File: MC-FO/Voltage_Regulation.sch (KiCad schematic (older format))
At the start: 2 parts

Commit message: Add files via upload
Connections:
- net GND renamed GND1
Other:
- note added: "add comparatorson both and logically AND together for LED on power status\n\n\n (windowed comparators or voltage supervisors)"
- note added: "zach planning on adding caps. Pi Filter"
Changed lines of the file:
@@
 $Descr A4 11693 8268
 encoding utf-8
-Sheet 2 12
+Sheet 11 11
 Title ""
 Date ""
@@
 Wire Wire Line
 	3600 5150 4150 5150
-Text GLabel 4150 5150 2    50   Input ~ 0
-5V
-$Comp
-L power:GND #PWR?
-U 1 1 61717715
-P 3300 4900
-F 0 "#PWR?" H 3300 4650 50  0001 C CNN
-F 1 "GND" H 3305 4727 50  0000 C CNN
-F 2 "" H 3300 4900 50  0001 C CNN
-F 3 "" H 3300 4900 50  0001 C CNN
-	1    3300 4900
-	1    0    0    -1
-$EndComp
 Wire Wire Line
 	5950 4700 5650 4700
@@
 Wire Wire Line
 	5950 5150 6500 5150
-Text GLabel 6500 5150 2    50   Input ~ 0
-3V3
-$Comp
-L power:GND #PWR?
-U 1 1 6171CE7D
-P 5650 4900
-F 0 "#PWR?" H 5650 4650 50  0001 C CNN
-F 1 "GND" H 5655 4727 50  0000 C CNN
-F 2 "" H 5650 4900 50  0001 C CNN
-F 3 "" H 5650 4900 50  0001 C CNN
-	1    5650 4900
-	1    0    0    -1
-$EndComp
 $Comp
 L R-78E3.3-0.5:R-78E3.3-0.5 T?
@@
 Text HLabel 4750 3900 0    50   Input ~ 0
 Vdd
+Text Notes 3700 2550 2    50   ~ 0
+add comparatorson both and logically AND together for LED on power status\n\n\n (windowed comparators or voltage supervisors)
+Text Notes 2550 3650 2    50   ~ 0
+zach planning on adding caps. Pi Filter
+Text HLabel 6500 5150 2    50   Input ~ 0
+3V3
+Text HLabel 4150 5150 2    50   Input ~ 0
+5V
+Text HLabel 3300 4900 0    50   Input ~ 0
+GND1
+Text HLabel 5650 4900 0    50   Input ~ 0
+GND1
 $EndSCHEMATC

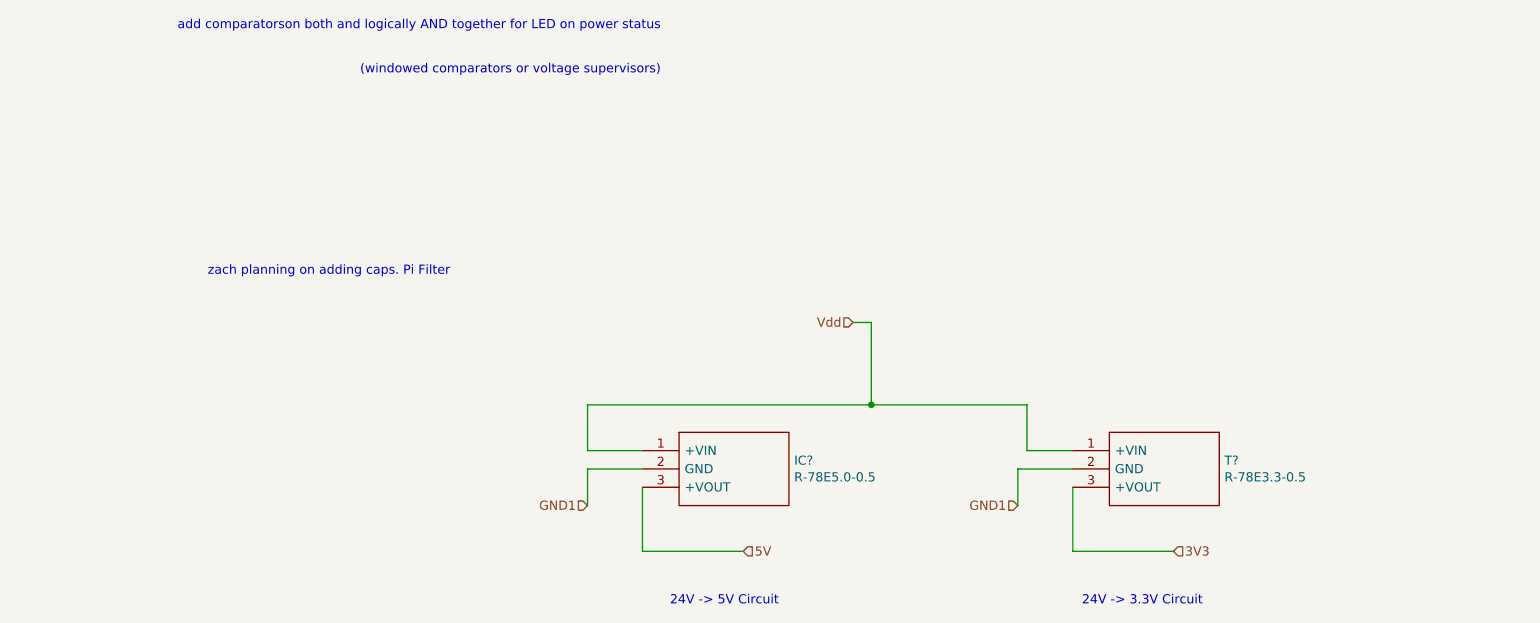
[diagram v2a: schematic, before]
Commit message: Updated naming, Pi filters
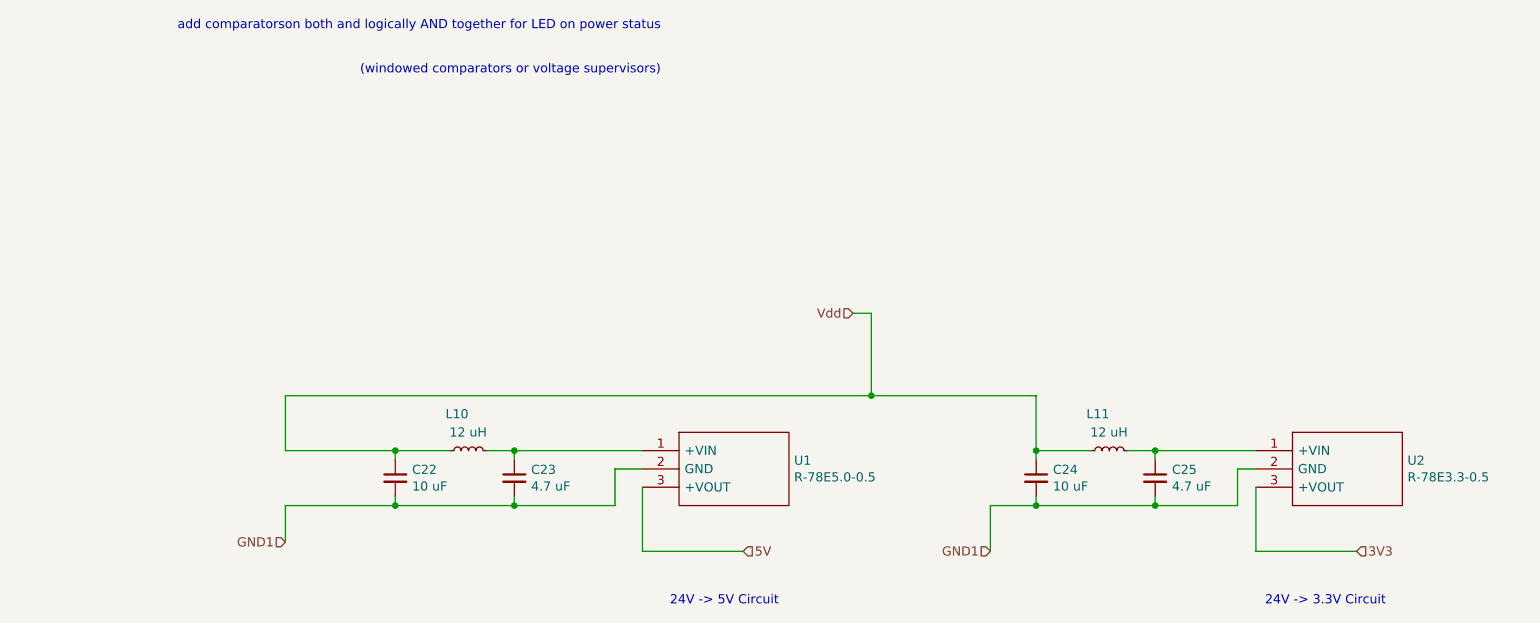
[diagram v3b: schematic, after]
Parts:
- added C22, C24: 10 uF, symbol Device:C_Small
- added C23, C25: 4.7 uF, symbol Device:C_Small
- added L10, L11: 12 uH, symbol Device:L_Small
- gave numbers to parts that had none: 2
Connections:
- net GND1: now also C22.2, C23.2, C24.2, C25.2
- net Vdd: now also C22.1, C24.1, L10.1, L11.1; no longer U1.1 (+VIN), U2.1 (+VIN)
- new net: C23.1, L10.2, U1.1 (+VIN)
- new net: C25.1, L11.2, U2.1 (+VIN)
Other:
- note removed: "zach planning on adding caps. Pi Filter"
- moved on the sheet: U2
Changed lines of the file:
@@
 $Descr A4 11693 8268
 encoding utf-8
-Sheet 11 11
+Sheet 10 11
 Title ""
 Date ""
@@
 Text Notes 3750 5450 0    50   ~ 0
 24V -> 5V Circuit
-Text Notes 6000 5450 0    50   ~ 0
+Text Notes 7000 5450 0    50   ~ 0
 24V -> 3.3V Circuit
 $Comp
@@
 U 1 1 61715B51
 P 3600 4600
-F 0 "IC?" H 4428 4546 50  0000 L CNN
+AR Path="/61715B51" Ref="IC?"  Part="1"
+AR Path="/6175C442/61715B51" Ref="U1"  Part="1"
+F 0 "U1" H 4428 4546 50  0000 L CNN
 F 1 "R-78E5.0-0.5" H 4428 4455 50  0000 L CNN
 F 2 "R78E5005" H 4450 4700 50  0001 L CNN
@@
 $EndComp
 Wire Wire Line
-	3600 4700 3300 4700
-Wire Wire Line
-	3300 4700 3300 4900
+	1650 4900 1650 5100
 Wire Wire Line
 	3600 4800 3600 5150
@@
 	3600 5150 4150 5150
 Wire Wire Line
-	5950 4700 5650 4700
-Wire Wire Line
-	5650 4700 5650 4900
-Wire Wire Line
-	5950 4800 5950 5150
-Wire Wire Line
-	5950 5150 6500 5150
+	6950 4800 6950 5150
+Wire Wire Line
+	6950 5150 7500 5150
 $Comp
 L R-78E3.3-0.5:R-78E3.3-0.5 T?
 U 1 1 6171D286
-P 5950 4600
-F 0 "T?" H 6778 4546 50  0000 L CNN
-F 1 "R-78E3.3-0.5" H 6778 4455 50  0000 L CNN
-F 2 "R78E1205" H 6800 4700 50  0001 L CNN
-F 3 "http://www.recom-power.com/pdf/Innoline/R-78Exx-0.5.pdf" H 6800 4600 50  0001 L CNN
-	1    5950 4600
-	1    0    0    -1
-$EndComp
-Wire Wire Line
-	4750 3900 4850 3900
-Wire Wire Line
-	4850 3900 4850 4350
-Wire Wire Line
-	4850 4350 3300 4350
-Wire Wire Line
-	3300 4350 3300 4600
-Wire Wire Line
-	3300 4600 3600 4600
-Wire Wire Line
-	4850 4350 5700 4350
-Wire Wire Line
-	5700 4350 5700 4600
-Connection ~ 4850 4350
-Wire Wire Line
-	5700 4600 5950 4600
-Text HLabel 4750 3900 0    50   Input ~ 0
+P 6950 4600
+AR Path="/6171D286" Ref="T?"  Part="1"
+AR Path="/6175C442/6171D286" Ref="U2"  Part="1"
+F 0 "U2" H 7778 4546 50  0000 L CNN
+F 1 "R-78E3.3-0.5" H 7778 4455 50  0000 L CNN
+F 2 "R78E1205" H 7800 4700 50  0001 L CNN
+F 3 "http://www.recom-power.com/pdf/Innoline/R-78Exx-0.5.pdf" H 7800 4600 50  0001 L CNN
+	1    6950 4600
+	1    0    0    -1
+$EndComp
+Wire Wire Line
+	4750 3850 4850 3850
+Wire Wire Line
+	4850 3850 4850 4300
+Connection ~ 4850 4300
+Text HLabel 4750 3850 0    50   Input ~ 0
 Vdd
 Text Notes 3700 2550 2    50   ~ 0
 add comparatorson both and logically AND together for LED on power status\n\n\n (windowed comparators or voltage supervisors)
-Text Notes 2550 3650 2    50   ~ 0
-zach planning on adding caps. Pi Filter
-Text HLabel 6500 5150 2    50   Input ~ 0
+Text HLabel 7500 5150 2    50   Input ~ 0
 3V3
 Text HLabel 4150 5150 2    50   Input ~ 0
 5V
-Text HLabel 3300 4900 0    50   Input ~ 0
+Text HLabel 1650 5100 0    50   Input ~ 0
 GND1
-Text HLabel 5650 4900 0    50   Input ~ 0
+Text HLabel 5500 5150 0    50   Input ~ 0
 GND1
+$Comp
+L Device:C_Small C22
+U 1 1 61765AF4
+P 2250 4750
+F 0 "C22" H 2342 4796 50  0000 L CNN
+F 1 "10 uF" H 2342 4705 50  0000 L CNN
+F 2 "" H 2250 4750 50  0001 C CNN
+F 3 "~" H 2250 4750 50  0001 C CNN
+	1    2250 4750
+	1    0    0    -1
+$EndComp
+$Comp
+L Device:C_Small C23
+U 1 1 61766D82
+P 2900 4750
+F 0 "C23" H 2992 4796 50  0000 L CNN
+F 1 "4.7 uF" H 2992 4705 50  0000 L CNN
+F 2 "" H 2900 4750 50  0001 C CNN
+F 3 "~" H 2900 4750 50  0001 C CNN
+	1    2900 4750
+	1    0    0    -1
+$EndComp
+$Comp
+L Device:L_Small L10
+U 1 1 61767909
+P 2650 4600
+F 0 "L10" V 2850 4600 50  0000 L CNN
+F 1 "12 uH" V 2750 4500 50  0000 L CNN
+F 2 "" H 2650 4600 50  0001 C CNN
+F 3 "~" H 2650 4600 50  0001 C CNN
+	1    2650 4600
+	0    -1   -1   0
+$EndComp
+Wire Wire Line
+	1650 4300 4850 4300
+Wire Wire Line
+	2550 4600 2250 4600
+Wire Wire Line
+	2250 4600 2250 4650
+Wire Wire Line
+	2250 4600 1650 4600
+Connection ~ 2250 4600
+Wire Wire Line
+	2750 4600 2900 4600
+Wire Wire Line
+	2900 4600 2900 4650
+Wire Wire Line
+	2900 4600 3600 4600
+Connection ~ 2900 4600
+Wire Wire Line
+	2250 4900 2250 4850
+Wire Wire Line
+	1650 4900 2250 4900
+Wire Wire Line
+	2250 4900 2900 4900
+Wire Wire Line
+	2900 4900 2900 4850
+Connection ~ 2250 4900
+Wire Wire Line
+	2900 4900 3450 4900
+Wire Wire Line
+	3450 4900 3450 4700
+Wire Wire Line
+	3450 4700 3600 4700
+Connection ~ 2900 4900
+Wire Wire Line
+	1650 4300 1650 4600
+$Comp
+L Device:C_Small C24
+U 1 1 61773A69
+P 5750 4750
+F 0 "C24" H 5842 4796 50  0000 L CNN
+F 1 "10 uF" H 5842 4705 50  0000 L CNN
+F 2 "" H 5750 4750 50  0001 C CNN
+F 3 "~" H 5750 4750 50  0001 C CNN
+	1    5750 4750
+	1    0    0    -1
+$EndComp
+$Comp
+L Device:C_Small C25
+U 1 1 61773ADF
+P 6400 4750
+F 0 "C25" H 6492 4796 50  0000 L CNN
+F 1 "4.7 uF" H 6492 4705 50  0000 L CNN
+F 2 "" H 6400 4750 50  0001 C CNN
+F 3 "~" H 6400 4750 50  0001 C CNN
+	1    6400 4750
+	1    0    0    -1
+$EndComp
+$Comp
+L Device:L_Small L11
+U 1 1 61773AE9
+P 6150 4600
+F 0 "L11" V 6350 4600 50  0000 L CNN
+F 1 "12 uH" V 6250 4500 50  0000 L CNN
+F 2 "" H 6150 4600 50  0001 C CNN
+F 3 "~" H 6150 4600 50  0001 C CNN
+	1    6150 4600
+	0    -1   -1   0
+$EndComp
+Wire Wire Line
+	6050 4600 5750 4600
+Wire Wire Line
+	5750 4600 5750 4650
+Wire Wire Line
+	6250 4600 6400 4600
+Wire Wire Line
+	6400 4600 6400 4650
+Wire Wire Line
+	5750 4900 5750 4850
+Wire Wire Line
+	5750 4900 6400 4900
+Wire Wire Line
+	6400 4900 6400 4850
+Wire Wire Line
+	5500 4900 5750 4900
+Wire Wire Line
+	5500 4900 5500 5150
+Connection ~ 5750 4900
+Wire Wire Line
+	5750 4300 5750 4600
+Wire Wire Line
+	4850 4300 5750 4300
+Connection ~ 5750 4600
+Wire Wire Line
+	6400 4600 6950 4600
+Connection ~ 6400 4600
+Wire Wire Line
+	6400 4900 6850 4900
+Wire Wire Line
+	6850 4900 6850 4700
+Wire Wire Line
+	6850 4700 6950 4700
+Connection ~ 6400 4900
 $EndSCHEMATC

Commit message: Add files via upload
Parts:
- renumbered C22 to C31, C23 to C32, C24 to C33, C25 to C34, U1 to IC1, L10 to L1, L11 to L2, U2 to T1
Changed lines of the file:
@@
 P 3600 4600
 AR Path="/61715B51" Ref="IC?"  Part="1"
-AR Path="/6175C442/61715B51" Ref="U1"  Part="1"
-F 0 "U1" H 4428 4546 50  0000 L CNN
+AR Path="/6175C442/61715B51" Ref="IC1"  Part="1"
+F 0 "IC1" H 4428 4546 50  0000 L CNN
 F 1 "R-78E5.0-0.5" H 4428 4455 50  0000 L CNN
 F 2 "R78E5005" H 4450 4700 50  0001 L CNN
@@
 P 6950 4600
 AR Path="/6171D286" Ref="T?"  Part="1"
-AR Path="/6175C442/6171D286" Ref="U2"  Part="1"
-F 0 "U2" H 7778 4546 50  0000 L CNN
+AR Path="/6175C442/6171D286" Ref="T1"  Part="1"
+F 0 "T1" H 7778 4546 50  0000 L CNN
 F 1 "R-78E3.3-0.5" H 7778 4455 50  0000 L CNN
 F 2 "R78E1205" H 7800 4700 50  0001 L CNN
@@
 GND1
 $Comp
-L Device:C_Small C22
+L Device:C_Small C31
 U 1 1 61765AF4
 P 2250 4750
-F 0 "C22" H 2342 4796 50  0000 L CNN
+F 0 "C31" H 2342 4796 50  0000 L CNN
 F 1 "10 uF" H 2342 4705 50  0000 L CNN
 F 2 "" H 2250 4750 50  0001 C CNN
@@
 $EndComp
 $Comp
-L Device:C_Small C23
+L Device:C_Small C32
 U 1 1 61766D82
 P 2900 4750
-F 0 "C23" H 2992 4796 50  0000 L CNN
+F 0 "C32" H 2992 4796 50  0000 L CNN
 F 1 "4.7 uF" H 2992 4705 50  0000 L CNN
 F 2 "" H 2900 4750 50  0001 C CNN
@@
 $EndComp
 $Comp
-L Device:L_Small L10
+L Device:L_Small L1
 U 1 1 61767909
 P 2650 4600
-F 0 "L10" V 2850 4600 50  0000 L CNN
+F 0 "L1" V 2850 4600 50  0000 L CNN
 F 1 "12 uH" V 2750 4500 50  0000 L CNN
 F 2 "" H 2650 4600 50  0001 C CNN
@@
 	1650 4300 1650 4600
 $Comp
-L Device:C_Small C24
+L Device:C_Small C33
 U 1 1 61773A69
 P 5750 4750
-F 0 "C24" H 5842 4796 50  0000 L CNN
+F 0 "C33" H 5842 4796 50  0000 L CNN
 F 1 "10 uF" H 5842 4705 50  0000 L CNN
 F 2 "" H 5750 4750 50  0001 C CNN
@@
 $EndComp
 $Comp
-L Device:C_Small C25
+L Device:C_Small C34
 U 1 1 61773ADF
 P 6400 4750
-F 0 "C25" H 6492 4796 50  0000 L CNN
+F 0 "C34" H 6492 4796 50  0000 L CNN
 F 1 "4.7 uF" H 6492 4705 50  0000 L CNN
 F 2 "" H 6400 4750 50  0001 C CNN
@@
 $EndComp
 $Comp
-L Device:L_Small L11
+L Device:L_Small L2
 U 1 1 61773AE9
 P 6150 4600
-F 0 "L11" V 6350 4600 50  0000 L CNN
+F 0 "L2" V 6350 4600 50  0000 L CNN
 F 1 "12 uH" V 6250 4500 50  0000 L CNN
 F 2 "" H 6150 4600 50  0001 C CNN

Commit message: a few more FO tweaks 10-26
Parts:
- C31, C32, C33, C34: footprint (none) -> Capacitor_SMD:C_0603_1608Metric
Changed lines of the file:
@@
 F 0 "C31" H 2342 4796 50  0000 L CNN
 F 1 "10 uF" H 2342 4705 50  0000 L CNN
-F 2 "" H 2250 4750 50  0001 C CNN
+F 2 "Capacitor_SMD:C_0603_1608Metric" H 2250 4750 50  0001 C CNN
 F 3 "~" H 2250 4750 50  0001 C CNN
 	1    2250 4750
@@
 F 0 "C32" H 2992 4796 50  0000 L CNN
 F 1 "4.7 uF" H 2992 4705 50  0000 L CNN
-F 2 "" H 2900 4750 50  0001 C CNN
+F 2 "Capacitor_SMD:C_0603_1608Metric" H 2900 4750 50  0001 C CNN
 F 3 "~" H 2900 4750 50  0001 C CNN
 	1    2900 4750
@@
 F 0 "C33" H 5842 4796 50  0000 L CNN
 F 1 "10 uF" H 5842 4705 50  0000 L CNN
-F 2 "" H 5750 4750 50  0001 C CNN
+F 2 "Capacitor_SMD:C_0603_1608Metric" H 5750 4750 50  0001 C CNN
 F 3 "~" H 5750 4750 50  0001 C CNN
 	1    5750 4750
@@
 F 0 "C34" H 6492 4796 50  0000 L CNN
 F 1 "4.7 uF" H 6492 4705 50  0000 L CNN
-F 2 "" H 6400 4750 50  0001 C CNN
+F 2 "Capacitor_SMD:C_0603_1608Metric" H 6400 4750 50  0001 C CNN
 F 3 "~" H 6400 4750 50  0001 C CNN
 	1    6400 4750

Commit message: added footprints and reference
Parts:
- removed IC1: R-78E5.0-0.5, R78E5005, symbol R-78E5.0-0.5:R-78E5.0-0.5
- removed T1: R-78E3.3-0.5, R78E1205, symbol R-78E3.3-0.5:R-78E3.3-0.5
- added U19: R-78E5.0-0.5, Package_SIP:SIP3_11.6x8.5mm, symbol Existing_IC_Models:R-78E5.0-0.5
- added U20: R-78E3.3-0.5, Package_SIP:SIP3_11.6x8.5mm, symbol Existing_IC_Models:R-78E3.3-0.5
- L1, L2: footprint (none) -> Inductor_SMD:L_0603_1608Metric
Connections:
- net 3V3: now also U20.3 (+VOUT)
- net 5V: now also U19.3 (+VOUT)
- net GND1: now also U19.2 (GND), U20.2 (GND)
- net at C32.1, L1.2: now also U19.1 (+VIN)
- net at C34.1, L2.2: now also U20.1 (+VIN)
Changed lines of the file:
@@
 Text Notes 7000 5450 0    50   ~ 0
 24V -> 3.3V Circuit
-$Comp
-L R-78E5.0-0.5:R-78E5.0-0.5 IC?
-U 1 1 61715B51
-P 3600 4600
-AR Path="/61715B51" Ref="IC?"  Part="1"
-AR Path="/6175C442/61715B51" Ref="IC1"  Part="1"
-F 0 "IC1" H 4428 4546 50  0000 L CNN
-F 1 "R-78E5.0-0.5" H 4428 4455 50  0000 L CNN
-F 2 "R78E5005" H 4450 4700 50  0001 L CNN
-F 3 "http://docs-emea.rs-online.com/webdocs/10a2/0900766b810a2db7.pdf" H 4450 4600 50  0001 L CNN
-F 4 "Switching Regulator,7-28Vin,5Vout 0.5A Switching Regulator, 7" H 4450 4500 50  0001 L CNN "Description"
-F 5 "10.9" H 4450 4400 50  0001 L CNN "Height"
-F 6 "RECOM Power" H 4450 4300 50  0001 L CNN "Manufacturer_Name"
-F 7 "R-78E5.0-0.5" H 4450 4200 50  0001 L CNN "Manufacturer_Part_Number"
-F 8 "919-R-78E5.0-0.5" H 4450 4100 50  0001 L CNN "Mouser Part Number"
-F 9 "https://www.mouser.co.uk/ProductDetail/RECOM-Power/R-78E50-05?qs=JeAkOuORR2UvBuiB2kZVZQ%3D%3D" H 4450 4000 50  0001 L CNN "Mouser Price/Stock"
-F 10 "R-78E5.0-0.5" H 4450 3900 50  0001 L CNN "Arrow Part Number"
-F 11 "https://www.arrow.com/en/products/r-78e5.0-0.5/recom-power" H 4450 3800 50  0001 L CNN "Arrow Price/Stock"
-	1    3600 4600
-	1    0    0    -1
-$EndComp
 Wire Wire Line
 	1650 4900 1650 5100
@@
 Wire Wire Line
 	6950 5150 7500 5150
-$Comp
-L R-78E3.3-0.5:R-78E3.3-0.5 T?
-U 1 1 6171D286
-P 6950 4600
-AR Path="/6171D286" Ref="T?"  Part="1"
-AR Path="/6175C442/6171D286" Ref="T1"  Part="1"
-F 0 "T1" H 7778 4546 50  0000 L CNN
-F 1 "R-78E3.3-0.5" H 7778 4455 50  0000 L CNN
-F 2 "R78E1205" H 7800 4700 50  0001 L CNN
-F 3 "http://www.recom-power.com/pdf/Innoline/R-78Exx-0.5.pdf" H 7800 4600 50  0001 L CNN
-	1    6950 4600
-	1    0    0    -1
-$EndComp
 Wire Wire Line
 	4750 3850 4850 3850
@@
 F 0 "L1" V 2850 4600 50  0000 L CNN
 F 1 "12 uH" V 2750 4500 50  0000 L CNN
-F 2 "" H 2650 4600 50  0001 C CNN
+F 2 "Inductor_SMD:L_0603_1608Metric" H 2650 4600 50  0001 C CNN
 F 3 "~" H 2650 4600 50  0001 C CNN
 	1    2650 4600
@@
 F 0 "L2" V 6350 4600 50  0000 L CNN
 F 1 "12 uH" V 6250 4500 50  0000 L CNN
-F 2 "" H 6150 4600 50  0001 C CNN
+F 2 "Inductor_SMD:L_0603_1608Metric" H 6150 4600 50  0001 C CNN
 F 3 "~" H 6150 4600 50  0001 C CNN
 	1    6150 4600
@@
 	6850 4700 6950 4700
 Connection ~ 6400 4900
+$Comp
+L Existing_IC_Models:R-78E3.3-0.5 U20
+U 1 1 617858EA
+P 6950 4600
+F 0 "U20" H 7778 4546 50  0000 L CNN
+F 1 "R-78E3.3-0.5" H 7778 4455 50  0000 L CNN
+F 2 "Package_SIP:SIP3_11.6x8.5mm" H 7800 4700 50  0001 L CNN
+F 3 "http://www.recom-power.com/pdf/Innoline/R-78Exx-0.5.pdf" H 7800 4600 50  0001 L CNN
+F 4 "Switching Regulator 6-28Vin 3.3Vout 0.5A Switching Regulator, 6" H 7800 4500 50  0001 L CNN "Description"
+F 5 "10.9" H 7800 4400 50  0001 L CNN "Height"
+F 6 "RECOM Power" H 7800 4300 50  0001 L CNN "Manufacturer_Name"
+F 7 "R-78E3.3-0.5" H 7800 4200 50  0001 L CNN "Manufacturer_Part_Number"
+F 8 "919-R-78E3.3-0.5" H 7800 4100 50  0001 L CNN "Mouser Part Number"
+F 9 "https://www.mouser.co.uk/ProductDetail/RECOM-Power/R-78E33-05?qs=W2iVYWQZWNCE79Y%252BXUlz8Q%3D%3D" H 7800 4000 50  0001 L CNN "Mouser Price/Stock"
+F 10 "R-78E3.3-0.5" H 7800 3900 50  0001 L CNN "Arrow Part Number"
+F 11 "https://www.arrow.com/en/products/r-78e3.3-0.5/recom-power" H 7800 3800 50  0001 L CNN "Arrow Price/Stock"
+	1    6950 4600
+	1    0    0    -1
+$EndComp
+$Comp
+L Existing_IC_Models:R-78E5.0-0.5 U19
+U 1 1 617A1AF8
+P 3600 4600
+F 0 "U19" H 4428 4546 50  0000 L CNN
+F 1 "R-78E5.0-0.5" H 4428 4455 50  0000 L CNN
+F 2 "Package_SIP:SIP3_11.6x8.5mm" H 4450 4700 50  0001 L CNN
+F 3 "http://docs-emea.rs-online.com/webdocs/10a2/0900766b810a2db7.pdf" H 4450 4600 50  0001 L CNN
+F 4 "Switching Regulator,7-28Vin,5Vout 0.5A Switching Regulator, 7" H 4450 4500 50  0001 L CNN "Description"
+F 5 "10.9" H 4450 4400 50  0001 L CNN "Height"
+F 6 "RECOM Power" H 4450 4300 50  0001 L CNN "Manufacturer_Name"
+F 7 "R-78E5.0-0.5" H 4450 4200 50  0001 L CNN "Manufacturer_Part_Number"
+F 8 "919-R-78E5.0-0.5" H 4450 4100 50  0001 L CNN "Mouser Part Number"
+F 9 "https://www.mouser.co.uk/ProductDetail/RECOM-Power/R-78E50-05?qs=JeAkOuORR2UvBuiB2kZVZQ%3D%3D" H 4450 4000 50  0001 L CNN "Mouser Price/Stock"
+F 10 "R-78E5.0-0.5" H 4450 3900 50  0001 L CNN "Arrow Part Number"
+F 11 "https://www.arrow.com/en/products/r-78e5.0-0.5/recom-power" H 4450 3800 50  0001 L CNN "Arrow Price/Stock"
+	1    3600 4600
+	1    0    0    -1
+$EndComp
 $EndSCHEMATC
